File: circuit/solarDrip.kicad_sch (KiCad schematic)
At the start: 21 parts, among them J1 solar_charger, J2 battery, J3 solar_panel, J4 pump, J5 soil_moisture, J6 water_level, J7 USB_C_Receptacle_USB2.0_14P, Q1 2N7002K, Q2 2N7002K, U1 ESP32-C3_SUPERMINI

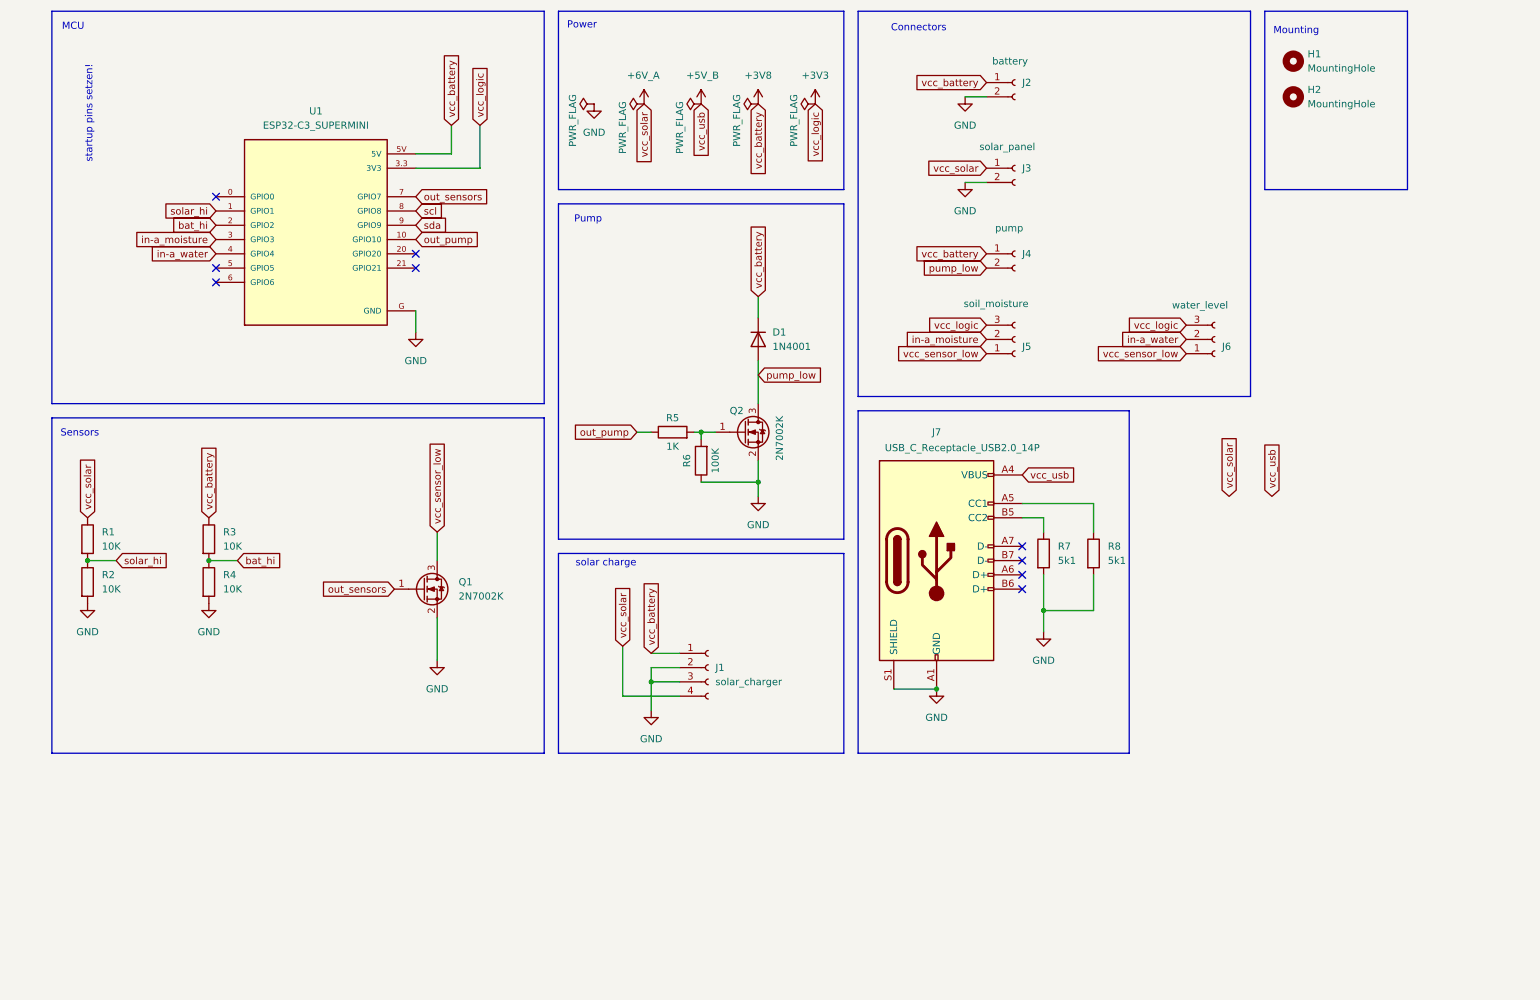
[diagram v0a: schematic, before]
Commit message: add power select circuit
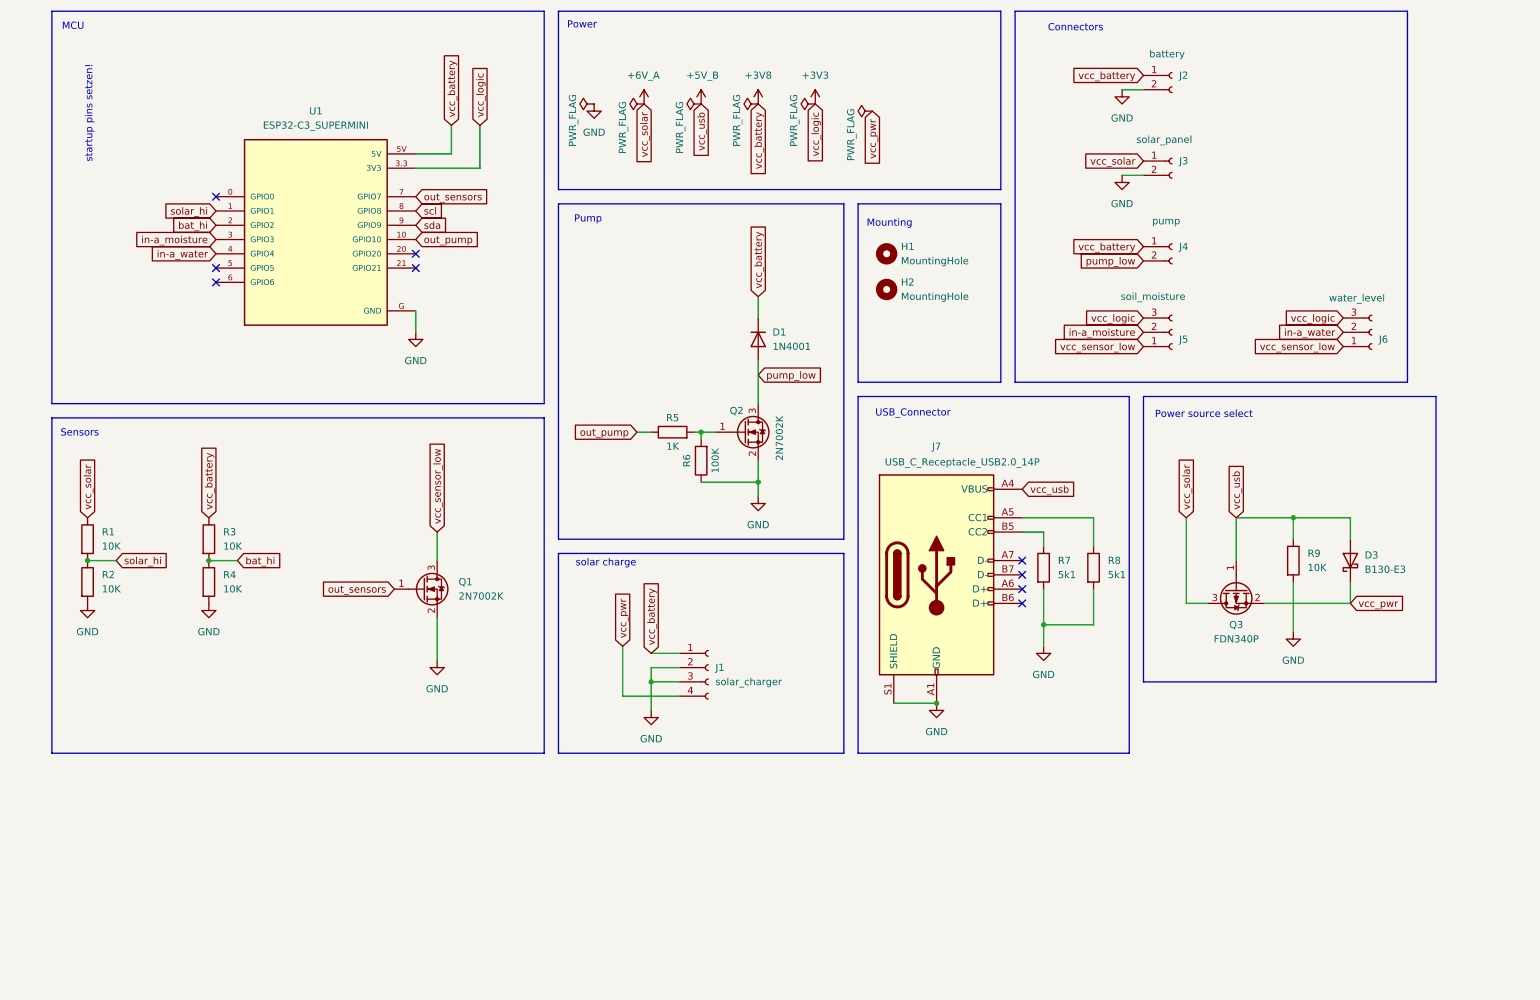
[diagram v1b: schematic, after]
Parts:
- added D3: B130-E3, Diode_SMD:D_SMA, symbol Diode:B130-E3
- added Q3: FDN340P, Package_TO_SOT_SMD:SOT-23, symbol Transistor_FET:FDN340P
- added R9: 10K, symbol Device:R
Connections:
- net +5V_B: now also D3.2 (A), Q3.1 (G), R9.1
- net +6V_A: now also Q3.3 (D); no longer J1.4 (Pin_4)
- net GND: now also R9.2
- new net vcc_pwr: D3.1 (K), J1.4 (Pin_4), Q3.2 (S)
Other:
- note added: "Power source select"
- note added: "USB_Connector"
- moved on the sheet: H1, H2, J2, J3, J4, J5, J6, J7, R7, R8

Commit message: first stab at pcb placement
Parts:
- J2: value battery -> batt
- J3: value solar_panel -> solar
- J5: value soil_moisture -> soil
- J6: value water_level -> water
- J7: footprint (none) -> Connector_USB:USB_C_Receptacle_G-Switch_GT-USB-7010ASV
- R7, R8, R9: footprint (none) -> Resistor_SMD:R_0402_1005Metric_Pad0.72x0.64mm_HandSolder
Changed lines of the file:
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@@
 			)
 		)
-		(property "Value" "soil_moisture"
+		(property "Value" "soil"
 			(at 210.566 67.31 0)
 			(effects
@@
 			)
 		)
-		(property "Footprint" ""
+		(property "Footprint" "Resistor_SMD:R_0402_1005Metric_Pad0.72x0.64mm_HandSolder"
 			(at 239.522 114.3 90)
 			(effects
@@
 			)
 		)
-		(property "Footprint" ""
+		(property "Footprint" "Connector_USB:USB_C_Receptacle_G-Switch_GT-USB-7010ASV"
 			(at 181.61 116.84 0)
 			(effects
@@
 			)
 		)
-		(property "Value" "water_level"
+		(property "Value" "water"
 			(at 247.65 67.564 0)
 			(effects
@@
 			)
 		)
-		(property "Footprint" ""
+		(property "Footprint" "Resistor_SMD:R_0402_1005Metric_Pad0.72x0.64mm_HandSolder"
 			(at 195.072 115.57 90)
 			(effects
@@
 			)
 		)
-		(property "Footprint" ""
+		(property "Footprint" "Resistor_SMD:R_0402_1005Metric_Pad0.72x0.64mm_HandSolder"
 			(at 203.962 115.57 90)
 			(effects
@@
 			)
 		)
-		(property "Value" "solar_panel"
+		(property "Value" "solar"
 			(at 213.36 39.37 0)
 			(effects
@@
 			)
 		)
-		(property "Value" "battery"
+		(property "Value" "batt"
 			(at 215.646 24.13 0)
 			(effects

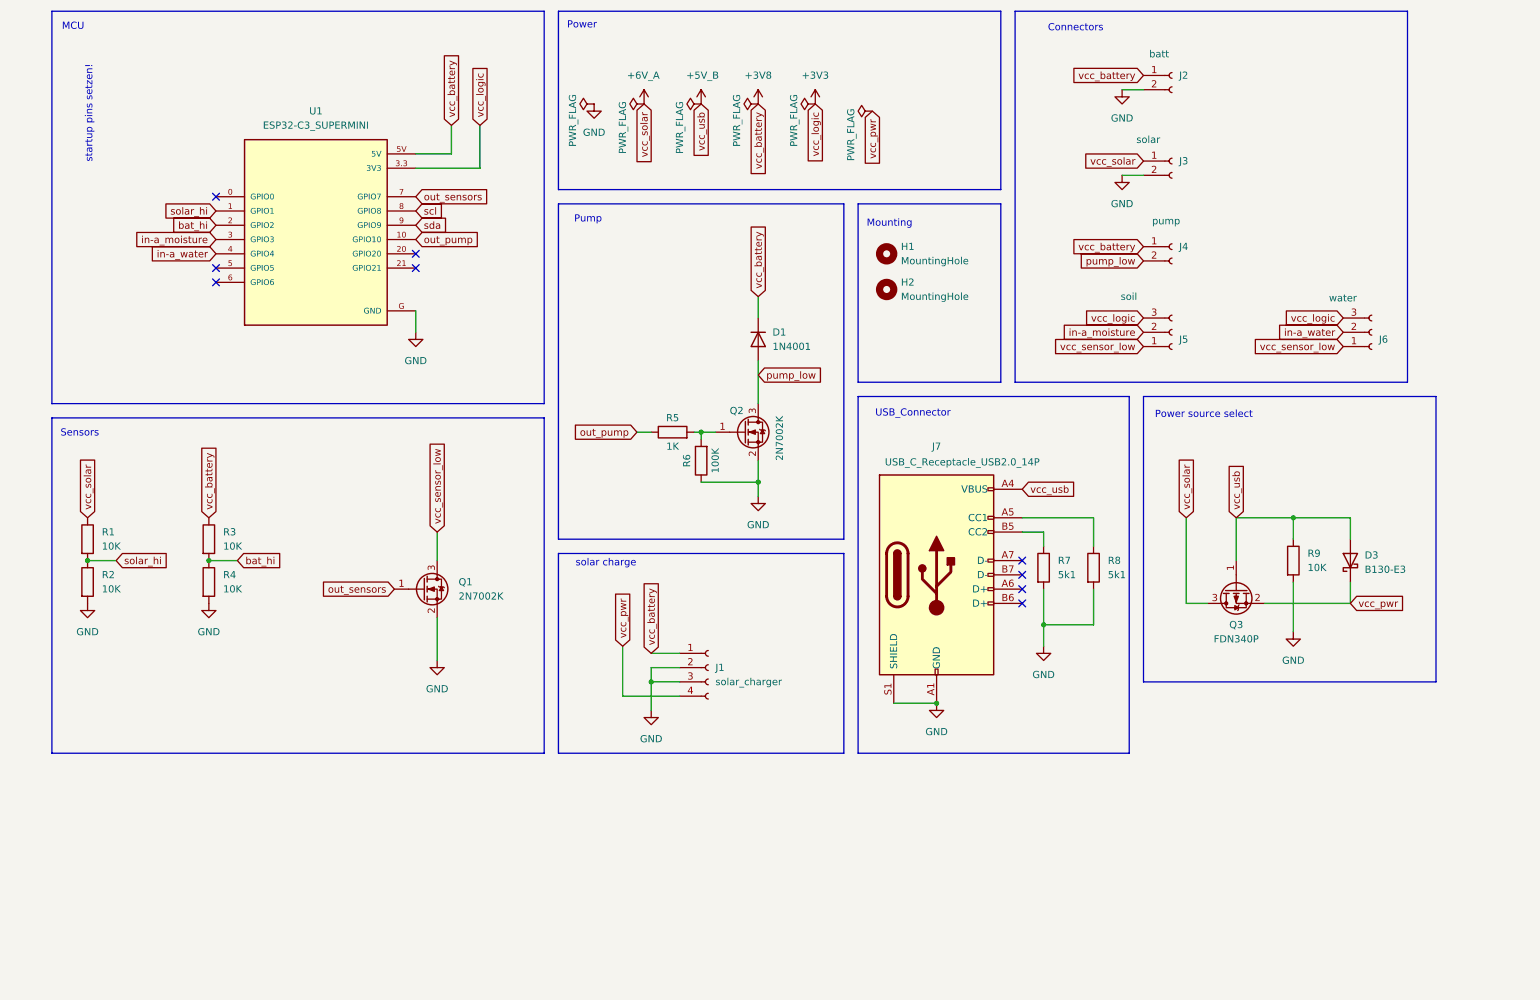
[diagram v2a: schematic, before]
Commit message: add testpoints & i2c to scematics
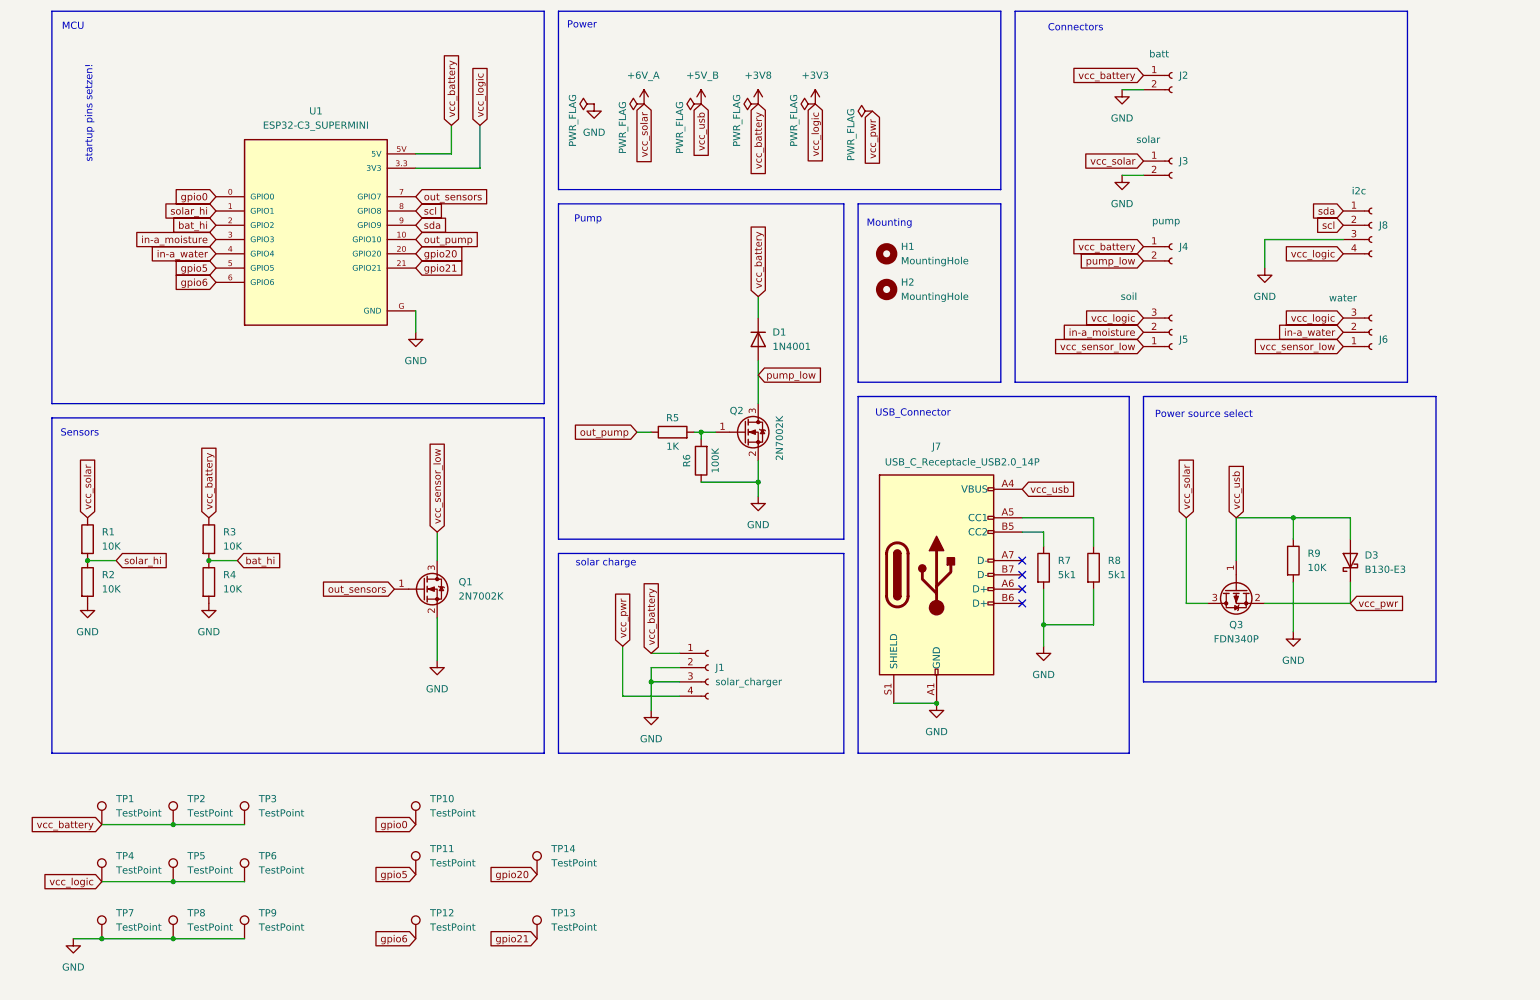
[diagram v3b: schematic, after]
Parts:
- added J8: i2c, symbol Connector:Conn_01x04_Socket
- added TP1, TP10, TP11, TP12, TP13, TP14, TP2, TP3, TP4, TP5, TP6, TP7, TP8, TP9: TestPoint, symbol Connector:TestPoint
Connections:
- net +3V3: now also J8.4 (Pin_4), TP4.1, TP5.1, TP6.1
- net +3V8: now also TP1.1, TP2.1, TP3.1
- net GND: now also J8.3 (Pin_3), TP7.1, TP8.1, TP9.1
- net scl: now also J8.2 (Pin_2)
- net sda: now also J8.1 (Pin_1)
- net gpio0: now reaches U1.0 (GPIO0)
- net gpio0: now also TP10.1
- net gpio20: now reaches U1.20 (GPIO20)
- net gpio20: now also TP14.1
- net gpio21: now reaches U1.21 (GPIO21)
- net gpio21: now also TP13.1
- net gpio5: now reaches U1.5 (GPIO5)
- net gpio5: now also TP11.1
- net gpio6: now reaches U1.6 (GPIO6)
- net gpio6: now also TP12.1
- no-connect marks 9 -> 4

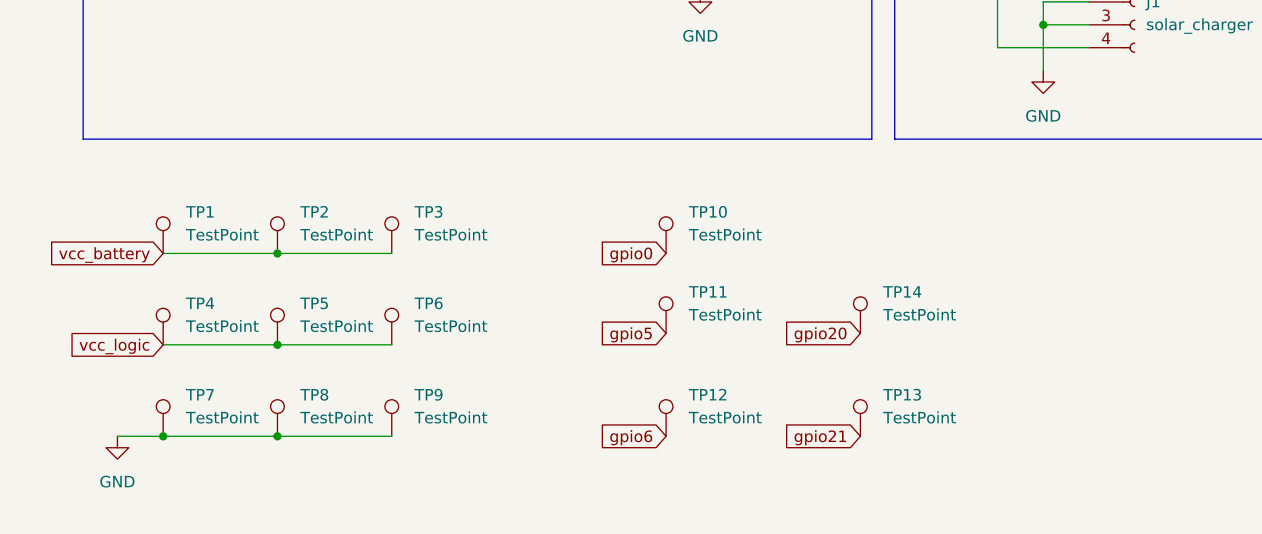
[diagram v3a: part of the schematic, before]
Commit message: vias, silkscreen, add usb_prw, logos and serials
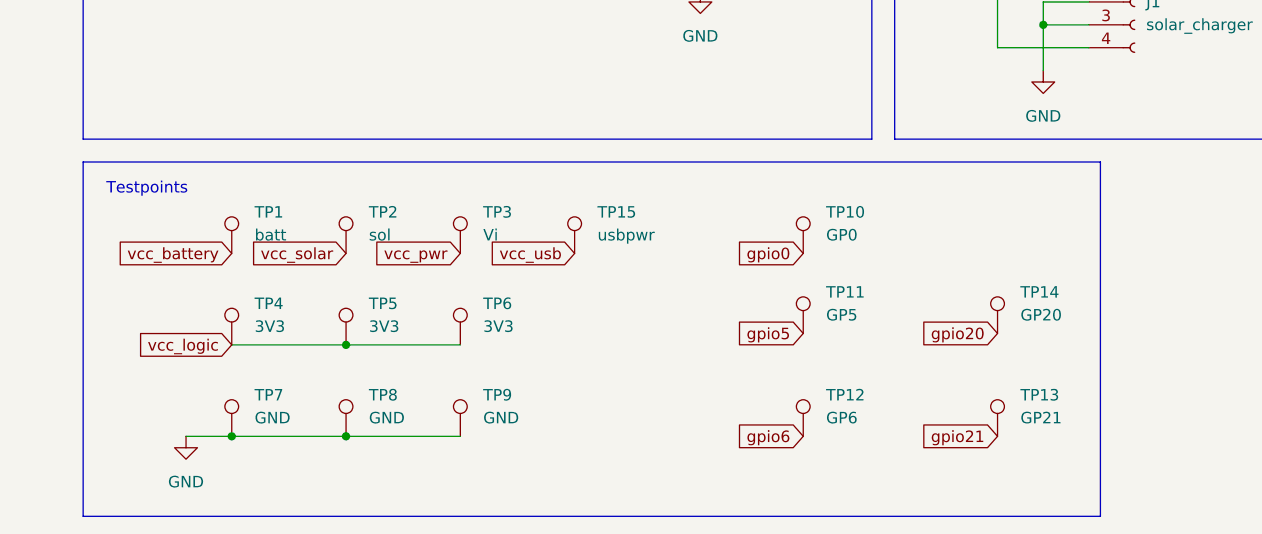
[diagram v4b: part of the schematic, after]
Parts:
- added TP15: usbpwr, TestPoint:TestPoint_Pad_D2.0mm, symbol Connector:TestPoint
- J8: footprint (none) -> Connector_JST:JST_PH_S4B-PH-K_1x04_P2.00mm_Horizontal
- TP1: value TestPoint -> batt; footprint (none) -> TestPoint:TestPoint_Pad_D2.0mm
- TP10: value TestPoint -> GP0; footprint (none) -> TestPoint:TestPoint_Pad_D2.0mm
- TP11: value TestPoint -> GP5; footprint (none) -> TestPoint:TestPoint_Pad_D2.0mm
- TP12: value TestPoint -> GP6; footprint (none) -> TestPoint:TestPoint_Pad_D2.0mm
- TP13: value TestPoint -> GP21; footprint (none) -> TestPoint:TestPoint_Pad_D2.0mm
- TP14: value TestPoint -> GP20; footprint (none) -> TestPoint:TestPoint_Pad_D2.0mm
- TP2: value TestPoint -> sol; footprint (none) -> TestPoint:TestPoint_Pad_D2.0mm
- TP3: value TestPoint -> Vi; footprint (none) -> TestPoint:TestPoint_Pad_D2.0mm
- TP4, TP5, TP6: value TestPoint -> 3V3; footprint (none) -> TestPoint:TestPoint_Pad_D2.0mm
- TP7, TP8, TP9: value TestPoint -> GND; footprint (none) -> TestPoint:TestPoint_Pad_2.0x2.0mm
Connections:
- net +3V8: no longer TP2.1, TP3.1
- net +5V_B: now also TP15.1
- net +6V_A: now also TP2.1
- net vcc_pwr: now also TP3.1
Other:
- note added: "Testpoints"
- moved on the sheet: TP1, TP10, TP11, TP12, TP13, TP14, TP2, TP3, TP4, TP5, TP6, TP7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

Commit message: add capacitor, cleanup
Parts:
- added C1: C_Polarized, Capacitor_THT:CP_Radial_D10.0mm_P7.50mm, symbol Device:C_Polarized
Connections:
- net +3V8: now also C1.1
- net GND: now also C1.2
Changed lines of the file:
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@@
 	)
 	(junction
+		(at 146.05 71.12)
+		(diameter 0)
+		(color 0 0 0 0)
+	)
+	(junction
 		(at 146.05 100.33)
 		(diameter 0)
@@
 	(wire
 		(pts
+			(xy 133.35 71.12) (xy 146.05 71.12)
+		)
+		(stroke
+			(width 0)
+			(type default)
+		)
+	)
+	(wire
+		(pts
 			(xy 121.92 138.43) (xy 132.08 138.43)
 		)
@@
 	)
 	(symbol
+		(lib_id "Device:C_Polarized")
+		(at 133.35 74.93 0)
+		(unit 1)
+		(exclude_from_sim no)
+		(in_bom yes)
+		(on_board yes)
+		(dnp no)
+		(property "Reference" "C1"
+			(at 137.16 72.7709 0)
+			(effects
+				(font
+					(size 1.27 1.27)
+				)
+				(justify left)
+			)
+		)
+		(property "Value" "C_Polarized"
+			(at 128.778 80.01 90)
+			(effects
+				(font
+					(size 1.27 1.27)
+				)
+				(justify left)
+			)
+		)
+		(property "Footprint" "Capacitor_THT:CP_Radial_D10.0mm_P7.50mm"
+			(at 134.3152 78.74 0)
+			(effects
+				(font
+					(size 1.27 1.27)
+				)
+				(hide yes)
+			)
+		)
+		(property "Datasheet" "~"
+			(at 133.35 74.93 0)
+			(effects
+				(font
+					(size 1.27 1.27)
+				)
+				(hide yes)
+			)
+		)
+		(property "Description" "Polarized capacitor"
+			(at 133.35 74.93 0)
+			(effects
+				(font
+					(size 1.27 1.27)
+				)
+				(hide yes)
+			)
+		)
+		(pin "1"
+		)
+		(pin "2"
+		)
+		(instances
+			(project "solarDrip"
+				(path "/6377a484-fa16-4056-97a2-452f2b7af807"
+					(reference "C1")
+					(unit 1)
+				)
+			)
+		)
+	)
+	(symbol
 		(lib_id "Connector:TestPoint")
 		(at 62.23 161.29 0)
@@
 					(unit 1)
 				)
+			)
+		)
+	)
+	(symbol
+		(lib_id "power:GND")
+		(at 133.35 78.74 0)
+		(unit 1)
+		(exclude_from_sim no)
+		(in_bom yes)
+		(on_board yes)
+		(dnp no)
+		(fields_autoplaced yes)
+		(property "Reference" "#PWR019"
+			(at 133.35 85.09 0)
+			(effects
+				(font
+					(size 1.27 1.27)
+				)
+				(hide yes)
+			)
+		)
+		(property "Value" "GND"
+			(at 133.35 83.82 0)
+			(effects
+				(font
+					(size 1.27 1.27)
+				)
+			)
+		)
+		(property "Footprint" ""
+			(at 133.35 78.74 0)
+			(effects
+				(font
+					(size 1.27 1.27)
+				)
+				(hide yes)
+			)
+		)
+		(property "Datasheet" ""
+			(at 133.35 78.74 0)
+			(effects
+				(font
+					(size 1.27 1.27)
+				)
+				(hide yes)
+			)
+		)
+		(property "Description" "Power symbol creates a global label with name \"GND\" , ground"
+			(at 133.35 78.74 0)
+			(effects
+				(font
+					(size 1.27 1.27)
+				)
+				(hide yes)
+			)
+		)
+		(pin "1"
+		)
+		(instances
+			(project "solarDrip"
+				(path "/6377a484-fa16-4056-97a2-452f2b7af807"
+					(reference "#PWR019")
+					(unit 1)
+				)
